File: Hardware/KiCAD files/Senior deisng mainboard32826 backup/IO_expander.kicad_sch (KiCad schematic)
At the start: 0 parts

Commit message: IO pull resistors, Motor driver V1, LCD communication
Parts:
- added D5: BAT54C, Package_TO_SOT_SMD:SOT-23, symbol Diode:BAT54C
- added R107, R137, R89, R90, R91, R92: 4K7, Resistor_SMD:R_0402_1005Metric_Wbry, symbol Device:R_Small
- added R7: 10K 0.2W, Resistor_SMD:R_0603_1608Metric_Wbry, symbol Device:R_Small
- added R8: 27K 0.1W, Resistor_SMD:R_0402_1005Metric_Wbry, symbol Device:R_Small
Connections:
- new net +3.3V: D5.3, R8.2
- new net DRIVER_0_STEP: R107.1, R137.1, R89.1, R90.1, R91.1, R92.1
- new net GND: R107.2, R137.2, R89.2, R90.2, R91.2, R92.2
- new net IO_0: D5.1, R7.1
- new net IO_0_IN: R7.2, R8.1
- new net IO_1: D5.2
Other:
- note added: "DRV Step Pulldowns"
- note added: "double check these values"
- note added: "parrallel to the drivers"

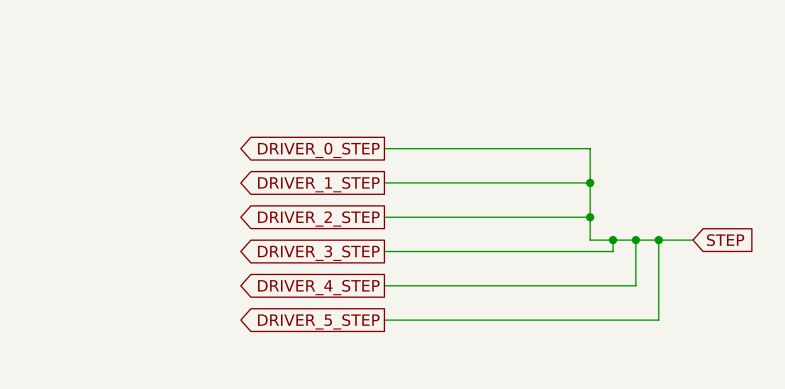
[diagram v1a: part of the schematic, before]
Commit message: 1.1, devices have been cleaned up
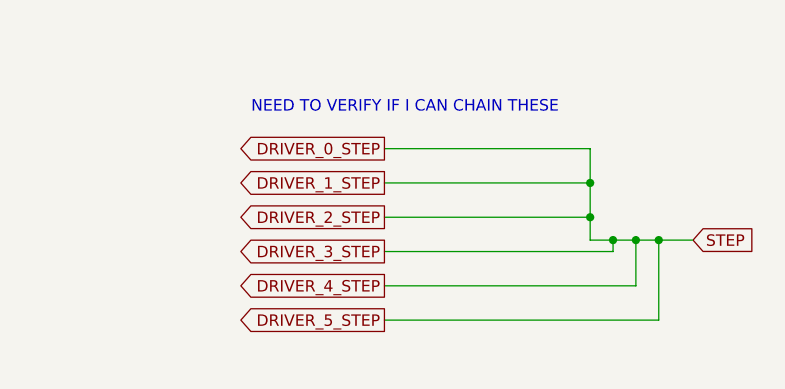
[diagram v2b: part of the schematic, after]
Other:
- note added: "NEED TO VERIFY IF I CAN CHAIN THESE"
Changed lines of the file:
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@@
 	(generator_version "10.0")
 	(paper "A4")
+	(text "NEED TO VERIFY IF I CAN CHAIN THESE\n"
+		(exclude_from_sim no)
+		(at 238.506 24.638 0)
+		(effects
+			(font
+				(size 1.27 1.27)
+			)
+		)
+	)
 	(text "parrallel to the drivers\n"
 		(exclude_from_sim no)

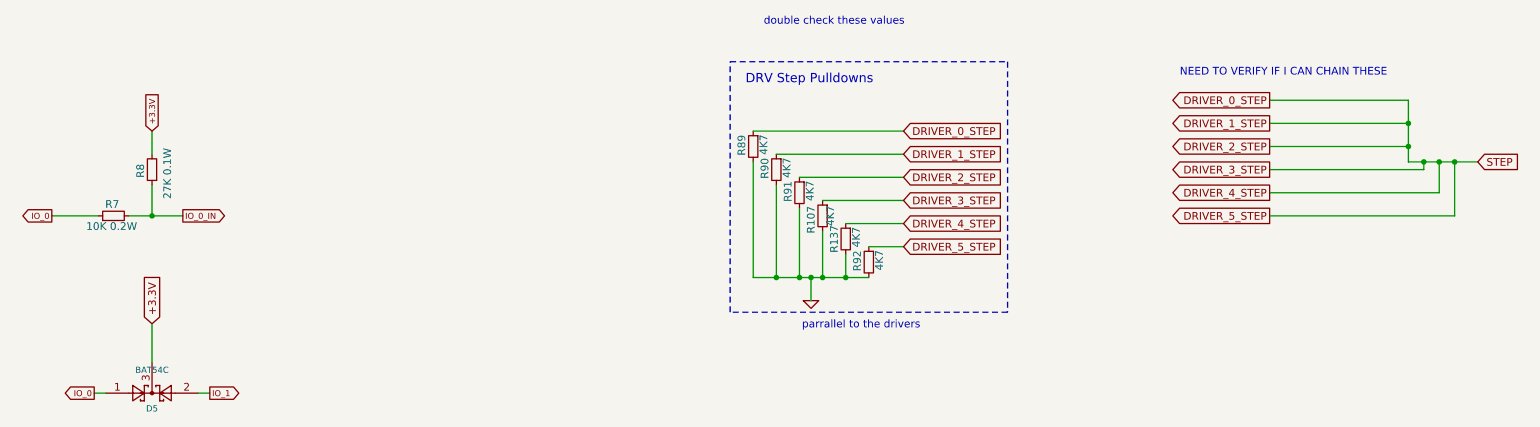
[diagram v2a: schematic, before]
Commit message: New project made to reflect layouts
New project files made in order to generate accurate layouts and create neatness.
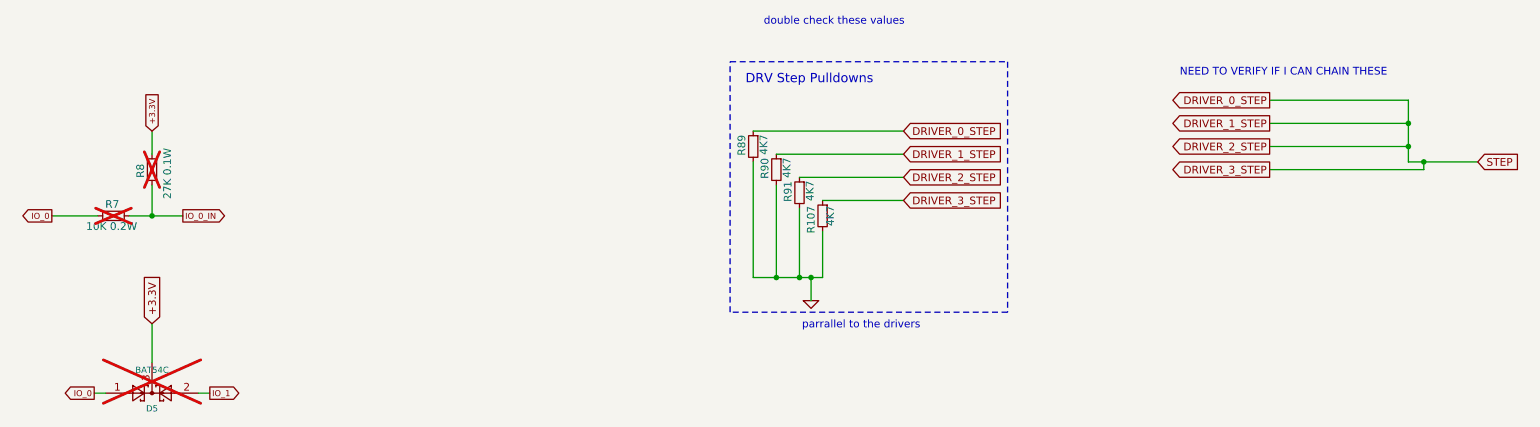
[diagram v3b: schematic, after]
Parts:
- removed R137, R92: 4K7, Resistor_SMD:R_0402_1005Metric_Wbry, symbol Device:R_Small
- D5, R7, R8: now not fitted
